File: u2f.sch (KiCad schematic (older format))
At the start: 1 part

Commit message: added some new footprints and stuff.
I'm having issues connecting everything up while keeping my optimal dimensions.
Options are to
- switch around some the GPIO pins (for LED) to avoid having traces run accross components
- Remove resistor and offload it to only when I'm programming (or directly wire D- and VCC to a "resistor", which will only be there during programmin)
- Remove programming pins and pre-program chip before putting it on the board (then I'd have to design a programmer PCB)
- (nucelar option) add an extra layer (basically two because I've never heard of a 3-layer PCB)
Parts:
- removed U?: ch554T, symbol ch554T
- added C1: C, Capacitors_SMD:C_0805_HandSoldering, symbol C
- added D1: LED, LEDs:LED_0805, symbol LED
- added P1: Touch Button, u2f:EdgeTouch, symbol CONN_01X01
- added P2: V33prog, Wire_Pads:SolderWirePad_single_0-8mmDrill, symbol CONN_01X01
- added P3: D- prog, Wire_Pads:SolderWirePad_single_0-8mmDrill, symbol CONN_01X01
- added P4: USB_A, symbol USB_A
- added R1: R, Resistors_SMD:R_0805_HandSoldering, symbol R
- added U1: ch552T, Housings_SSOP:TSSOP-20_4.4x6.5mm_Pitch0.65mm, symbol ch552T
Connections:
- net labels added: +5V, GND
- wire segments 0 -> 13
- no-connect marks 0 -> 13
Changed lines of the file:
@@
 LIBS:valves
 LIBS:ch554t
+LIBS:ch552t
+LIBS:usb_a
+LIBS:usbusb
+LIBS:u2f-cache
 EELAYER 25 0
 EELAYER END
@@
 $EndDescr
 $Comp
-L ch554T U?
-U 1 1 5CF7C254
-P 4350 3400
-F 0 "U?" V 4050 3400 60  0000 C CNN
-F 1 "ch554T" V 4500 3450 60  0000 C CNN
-F 2 "" V 4500 3450 60  0001 C CNN
-F 3 "" V 4500 3450 60  0001 C CNN
-	1    4350 3400
-	1    0    0    -1
+L ch552T U1
+U 1 1 5CF7CBDC
+P 5400 3650
+F 0 "U1" V 5100 3650 60  0000 C CNN
+F 1 "ch552T" V 5550 3700 60  0000 C CNN
+F 2 "Housings_SSOP:TSSOP-20_4.4x6.5mm_Pitch0.65mm" V 5550 3700 60  0001 C CNN
+F 3 "" V 5550 3700 60  0001 C CNN
+	1    5400 3650
+	1    0    0    -1
+$EndComp
+$Comp
+L LED D1
+U 1 1 5CF7CC1B
+P 6000 3900
+F 0 "D1" H 6000 4000 50  0000 C CNN
+F 1 "LED" H 6000 3800 50  0000 C CNN
+F 2 "LEDs:LED_0805" H 6000 3900 50  0001 C CNN
+F 3 "" H 6000 3900 50  0000 C CNN
+	1    6000 3900
+	-1   0    0    1
+$EndComp
+$Comp
+L GND #PWR3
+U 1 1 5CF7D104
+P 6150 3900
+F 0 "#PWR3" H 6150 3650 50  0001 C CNN
+F 1 "GND" H 6150 3750 50  0000 C CNN
+F 2 "" H 6150 3900 50  0000 C CNN
+F 3 "" H 6150 3900 50  0000 C CNN
+	1    6150 3900
+	0    -1   -1   0
+$EndComp
+$Comp
+L GND #PWR2
+U 1 1 5CF7D287
+P 5850 3400
+F 0 "#PWR2" H 5850 3150 50  0001 C CNN
+F 1 "GND" H 5850 3250 50  0000 C CNN
+F 2 "" H 5850 3400 50  0000 C CNN
+F 3 "" H 5850 3400 50  0000 C CNN
+	1    5850 3400
+	0    -1   -1   0
+$EndComp
+$Comp
+L +5V #PWR1
+U 1 1 5CF7D342
+P 5850 3300
+F 0 "#PWR1" H 5850 3150 50  0001 C CNN
+F 1 "+5V" H 5850 3440 50  0000 C CNN
+F 2 "" H 5850 3300 50  0000 C CNN
+F 3 "" H 5850 3300 50  0000 C CNN
+	1    5850 3300
+	0    1    1    0
+$EndComp
+$Comp
+L GND #PWR5
+U 1 1 5CF7D745
+P 7200 3650
+F 0 "#PWR5" H 7200 3400 50  0001 C CNN
+F 1 "GND" H 7200 3500 50  0000 C CNN
+F 2 "" H 7200 3650 50  0000 C CNN
+F 3 "" H 7200 3650 50  0000 C CNN
+	1    7200 3650
+	0    1    1    0
+$EndComp
+$Comp
+L +5V #PWR4
+U 1 1 5CF7D75F
+P 7200 3350
+F 0 "#PWR4" H 7200 3200 50  0001 C CNN
+F 1 "+5V" H 7200 3490 50  0000 C CNN
+F 2 "" H 7200 3350 50  0000 C CNN
+F 3 "" H 7200 3350 50  0000 C CNN
+	1    7200 3350
+	0    -1   -1   0
+$EndComp
+$Comp
+L +5V #PWR6
+U 1 1 5CF7D922
+P 8550 2850
+F 0 "#PWR6" H 8550 2700 50  0001 C CNN
+F 1 "+5V" H 8550 2990 50  0000 C CNN
+F 2 "" H 8550 2850 50  0000 C CNN
+F 3 "" H 8550 2850 50  0000 C CNN
+	1    8550 2850
+	1    0    0    -1
+$EndComp
+$Comp
+L C C1
+U 1 1 5CF7D93C
+P 8550 3000
+F 0 "C1" H 8575 3100 50  0000 L CNN
+F 1 "C" H 8575 2900 50  0000 L CNN
+F 2 "Capacitors_SMD:C_0805_HandSoldering" H 8588 2850 50  0001 C CNN
+F 3 "" H 8550 3000 50  0000 C CNN
+	1    8550 3000
+	1    0    0    -1
+$EndComp
+$Comp
+L GND #PWR7
+U 1 1 5CF7D969
+P 8550 3150
+F 0 "#PWR7" H 8550 2900 50  0001 C CNN
+F 1 "GND" H 8550 3000 50  0000 C CNN
+F 2 "" H 8550 3150 50  0000 C CNN
+F 3 "" H 8550 3150 50  0000 C CNN
+	1    8550 3150
+	1    0    0    -1
+$EndComp
+Wire Wire Line
+	7200 3550 6400 3550
+Wire Wire Line
+	6400 3550 6400 3800
+Wire Wire Line
+	6400 3800 5650 3800
+Wire Wire Line
+	5650 3700 6350 3700
+Wire Wire Line
+	6350 3700 6350 3450
+Wire Wire Line
+	6350 3450 7200 3450
+Wire Wire Line
+	4950 3800 3150 3800
+$Comp
+L CONN_01X01 P1
+U 1 1 5CF95DC3
+P 2950 3800
+F 0 "P1" H 2950 3900 50  0000 C CNN
+F 1 "Touch Button" V 3050 3800 50  0000 C CNN
+F 2 "u2f:EdgeTouch" H 2950 3800 50  0001 C CNN
+F 3 "" H 2950 3800 50  0000 C CNN
+	1    2950 3800
+	-1   0    0    1
+$EndComp
+Wire Wire Line
+	6600 3200 5650 3200
+Wire Wire Line
+	6600 2900 6600 3200
+$Comp
+L CONN_01X01 P2
+U 1 1 5CF95E72
+P 6600 2700
+F 0 "P2" H 6600 2800 50  0000 C CNN
+F 1 "V33prog" V 6700 2700 50  0000 C CNN
+F 2 "Wire_Pads:SolderWirePad_single_0-8mmDrill" H 6600 2700 50  0001 C CNN
+F 3 "" H 6600 2700 50  0000 C CNN
+	1    6600 2700
+	0    -1   -1   0
+$EndComp
+Wire Wire Line
+	6900 3450 6900 3050
+Connection ~ 6900 3450
+$Comp
+L R R1
+U 1 1 5CF95EDE
+P 6900 2900
+F 0 "R1" V 6980 2900 50  0000 C CNN
+F 1 "R" V 6900 2900 50  0000 C CNN
+F 2 "Resistors_SMD:R_0805_HandSoldering" V 6830 2900 50  0001 C CNN
+F 3 "" H 6900 2900 50  0000 C CNN
+	1    6900 2900
+	1    0    0    -1
+$EndComp
+$Comp
+L CONN_01X01 P3
+U 1 1 5CF95FF4
+P 7100 2750
+F 0 "P3" H 7100 2850 50  0000 C CNN
+F 1 "D- prog" V 7200 2750 50  0000 C CNN
+F 2 "Wire_Pads:SolderWirePad_single_0-8mmDrill" H 7100 2750 50  0001 C CNN
+F 3 "" H 7100 2750 50  0000 C CNN
+	1    7100 2750
+	1    0    0    -1
+$EndComp
+Wire Wire Line
+	5850 3900 5650 3900
+Wire Wire Line
+	5650 3300 5850 3300
+Wire Wire Line
+	5850 3400 5650 3400
+NoConn ~ 4950 3200
+NoConn ~ 4950 3300
+NoConn ~ 4950 3400
+NoConn ~ 4950 3500
+NoConn ~ 4950 3600
+NoConn ~ 4950 3700
+NoConn ~ 5650 3500
+NoConn ~ 5650 3600
+NoConn ~ 5650 4000
+NoConn ~ 5650 4100
+NoConn ~ 4950 4100
+NoConn ~ 4950 3900
+NoConn ~ 4950 4000
+$Comp
+L USB_A P4
+U 1 1 5CF97BF4
+P 7500 3550
+F 0 "P4" H 7700 3350 50  0000 C CNN
+F 1 "USB_A" H 7450 3750 50  0000 C CNN
+F 2 "" V 7450 3450 50  0000 C CNN
+F 3 "" V 7450 3450 50  0000 C CNN
+	1    7500 3550
+	0    1    1    0
 $EndComp
 $EndSCHEMATC

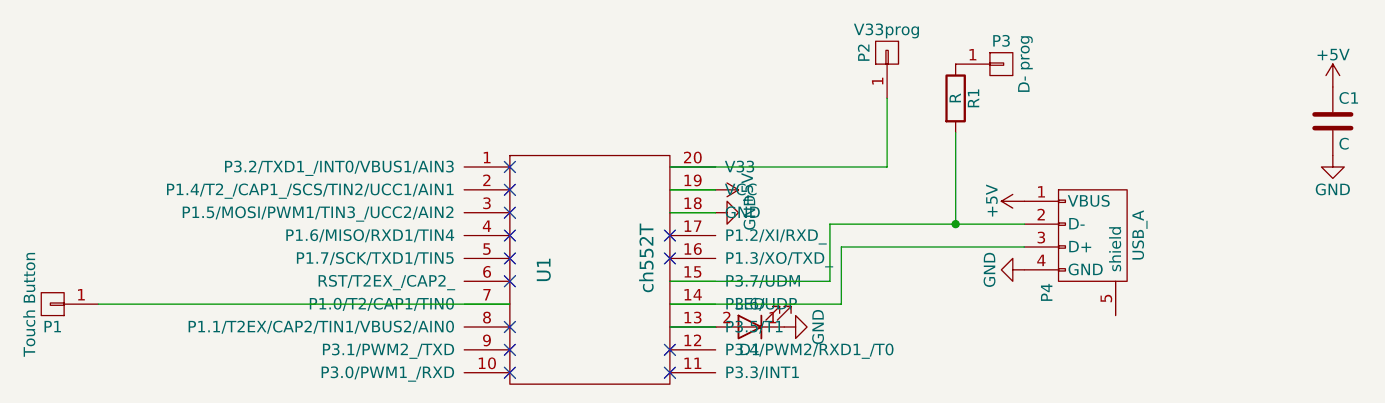
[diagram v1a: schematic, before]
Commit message: checking in code for tonight. It's def. not perfect I've removed pins from the IC footprint. The fact that this is a bad practice is not lost on me
I just need to re-route power and GND so that the USB actually fits the correct dimensions.

Once that is done I will work on edge cuts and look at some boardhouses to see who is willing to make this
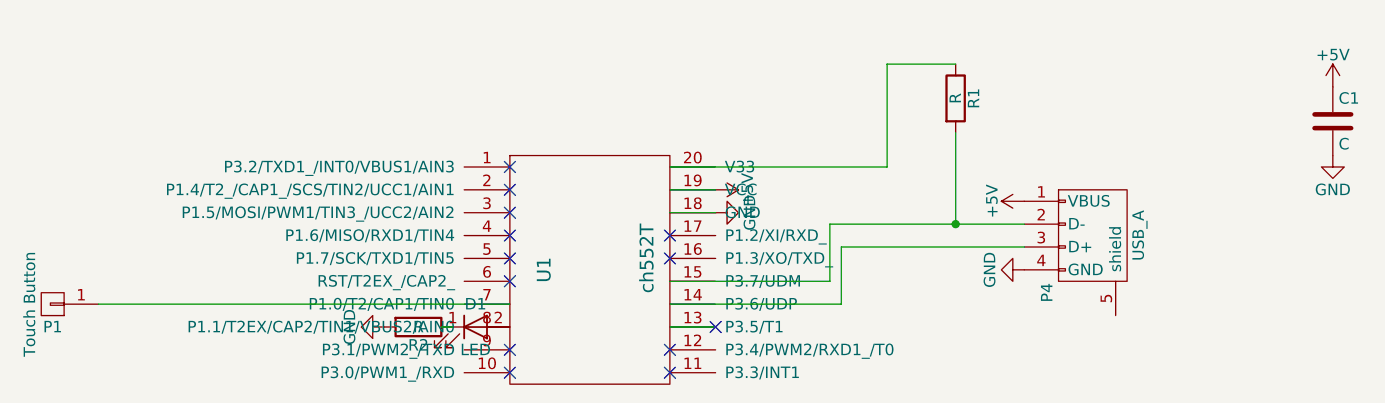
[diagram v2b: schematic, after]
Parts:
- removed P2: V33prog, Wire_Pads:SolderWirePad_single_0-8mmDrill, symbol CONN_01X01
- removed P3: D- prog, Wire_Pads:SolderWirePad_single_0-8mmDrill, symbol CONN_01X01
- added R2: R, Resistors_SMD:R_0805_HandSoldering, symbol R
- P4: footprint (none) -> u2f:USBEdge
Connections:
- net GND: now also R2.2; no longer D1.1 (K)
- net at U1.13 (P3.5/T1): no longer D1.2 (A)
- net at U1.20 (V33): now also R1.1
- net at U1.8 (P1.1/T2EX/CAP2/TIN1/VBUS2/AIN0): now also D1.2 (A)
- new net: D1.1 (K), R2.1
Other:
- moved on the sheet: D1
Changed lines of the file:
@@
 L LED D1
 U 1 1 5CF7CC1B
-P 6000 3900
-F 0 "D1" H 6000 4000 50  0000 C CNN
-F 1 "LED" H 6000 3800 50  0000 C CNN
-F 2 "LEDs:LED_0805" H 6000 3900 50  0001 C CNN
-F 3 "" H 6000 3900 50  0000 C CNN
-	1    6000 3900
-	-1   0    0    1
+P 4800 3900
+F 0 "D1" H 4800 4000 50  0000 C CNN
+F 1 "LED" H 4800 3800 50  0000 C CNN
+F 2 "LEDs:LED_0805" H 4800 3900 50  0001 C CNN
+F 3 "" H 4800 3900 50  0000 C CNN
+	1    4800 3900
+	1    0    0    -1
 $EndComp
 $Comp
-L GND #PWR3
-U 1 1 5CF7D104
-P 6150 3900
-F 0 "#PWR3" H 6150 3650 50  0001 C CNN
-F 1 "GND" H 6150 3750 50  0000 C CNN
-F 2 "" H 6150 3900 50  0000 C CNN
-F 3 "" H 6150 3900 50  0000 C CNN
-	1    6150 3900
-	0    -1   -1   0
-$EndComp
-$Comp
-L GND #PWR2
+L GND #PWR01
 U 1 1 5CF7D287
 P 5850 3400
-F 0 "#PWR2" H 5850 3150 50  0001 C CNN
+F 0 "#PWR01" H 5850 3150 50  0001 C CNN
 F 1 "GND" H 5850 3250 50  0000 C CNN
 F 2 "" H 5850 3400 50  0000 C CNN
@@
 $EndComp
 $Comp
-L +5V #PWR1
+L +5V #PWR02
 U 1 1 5CF7D342
 P 5850 3300
-F 0 "#PWR1" H 5850 3150 50  0001 C CNN
+F 0 "#PWR02" H 5850 3150 50  0001 C CNN
 F 1 "+5V" H 5850 3440 50  0000 C CNN
 F 2 "" H 5850 3300 50  0000 C CNN
@@
 $EndComp
 $Comp
-L GND #PWR5
+L GND #PWR03
 U 1 1 5CF7D745
 P 7200 3650
-F 0 "#PWR5" H 7200 3400 50  0001 C CNN
+F 0 "#PWR03" H 7200 3400 50  0001 C CNN
 F 1 "GND" H 7200 3500 50  0000 C CNN
 F 2 "" H 7200 3650 50  0000 C CNN
@@
 $EndComp
 $Comp
-L +5V #PWR4
+L +5V #PWR04
 U 1 1 5CF7D75F
 P 7200 3350
-F 0 "#PWR4" H 7200 3200 50  0001 C CNN
+F 0 "#PWR04" H 7200 3200 50  0001 C CNN
 F 1 "+5V" H 7200 3490 50  0000 C CNN
 F 2 "" H 7200 3350 50  0000 C CNN
@@
 $EndComp
 $Comp
-L +5V #PWR6
+L +5V #PWR05
 U 1 1 5CF7D922
 P 8550 2850
-F 0 "#PWR6" H 8550 2700 50  0001 C CNN
+F 0 "#PWR05" H 8550 2700 50  0001 C CNN
 F 1 "+5V" H 8550 2990 50  0000 C CNN
 F 2 "" H 8550 2850 50  0000 C CNN
@@
 $EndComp
 $Comp
-L GND #PWR7
+L GND #PWR06
 U 1 1 5CF7D969
 P 8550 3150
-F 0 "#PWR7" H 8550 2900 50  0001 C CNN
+F 0 "#PWR06" H 8550 2900 50  0001 C CNN
 F 1 "GND" H 8550 3000 50  0000 C CNN
 F 2 "" H 8550 3150 50  0000 C CNN
@@
 	6600 3200 5650 3200
 Wire Wire Line
-	6600 2900 6600 3200
-$Comp
-L CONN_01X01 P2
-U 1 1 5CF95E72
-P 6600 2700
-F 0 "P2" H 6600 2800 50  0000 C CNN
-F 1 "V33prog" V 6700 2700 50  0000 C CNN
-F 2 "Wire_Pads:SolderWirePad_single_0-8mmDrill" H 6600 2700 50  0001 C CNN
-F 3 "" H 6600 2700 50  0000 C CNN
-	1    6600 2700
-	0    -1   -1   0
-$EndComp
+	6600 2750 6600 3200
 Wire Wire Line
 	6900 3450 6900 3050
@@
 F 3 "" H 6900 2900 50  0000 C CNN
 	1    6900 2900
-	1    0    0    -1
-$EndComp
-$Comp
-L CONN_01X01 P3
-U 1 1 5CF95FF4
-P 7100 2750
-F 0 "P3" H 7100 2850 50  0000 C CNN
-F 1 "D- prog" V 7200 2750 50  0000 C CNN
-F 2 "Wire_Pads:SolderWirePad_single_0-8mmDrill" H 7100 2750 50  0001 C CNN
-F 3 "" H 7100 2750 50  0000 C CNN
-	1    7100 2750
 	1    0    0    -1
 $EndComp
@@
 NoConn ~ 5650 4100
 NoConn ~ 4950 4100
-NoConn ~ 4950 3900
 NoConn ~ 4950 4000
 $Comp
@@
 F 0 "P4" H 7700 3350 50  0000 C CNN
 F 1 "USB_A" H 7450 3750 50  0000 C CNN
-F 2 "" V 7450 3450 50  0000 C CNN
+F 2 "u2f:USBEdge" V 7450 3450 50  0001 C CNN
 F 3 "" V 7450 3450 50  0000 C CNN
 	1    7500 3550
 	0    1    1    0
 $EndComp
+Wire Wire Line
+	6900 2750 6600 2750
+$Comp
+L R R2
+U 1 1 5CF99EE0
+P 4550 3900
+F 0 "R2" V 4630 3900 50  0000 C CNN
+F 1 "R" V 4550 3900 50  0000 C CNN
+F 2 "Resistors_SMD:R_0805_HandSoldering" V 4480 3900 50  0001 C CNN
+F 3 "" H 4550 3900 50  0000 C CNN
+	1    4550 3900
+	0    1    1    0
+$EndComp
+NoConn ~ 5850 3900
+$Comp
+L GND #PWR?
+U 1 1 5CF9C1BD
+P 4400 3900
+F 0 "#PWR?" H 4400 3650 50  0001 C CNN
+F 1 "GND" H 4400 3750 50  0000 C CNN
+F 2 "" H 4400 3900 50  0000 C CNN
+F 3 "" H 4400 3900 50  0000 C CNN
+	1    4400 3900
+	0    1    1    0
+$EndComp
+Wire Wire Line
+	4700 3900 4650 3900
 $EndSCHEMATC
